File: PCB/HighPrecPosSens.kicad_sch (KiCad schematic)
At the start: 46 parts

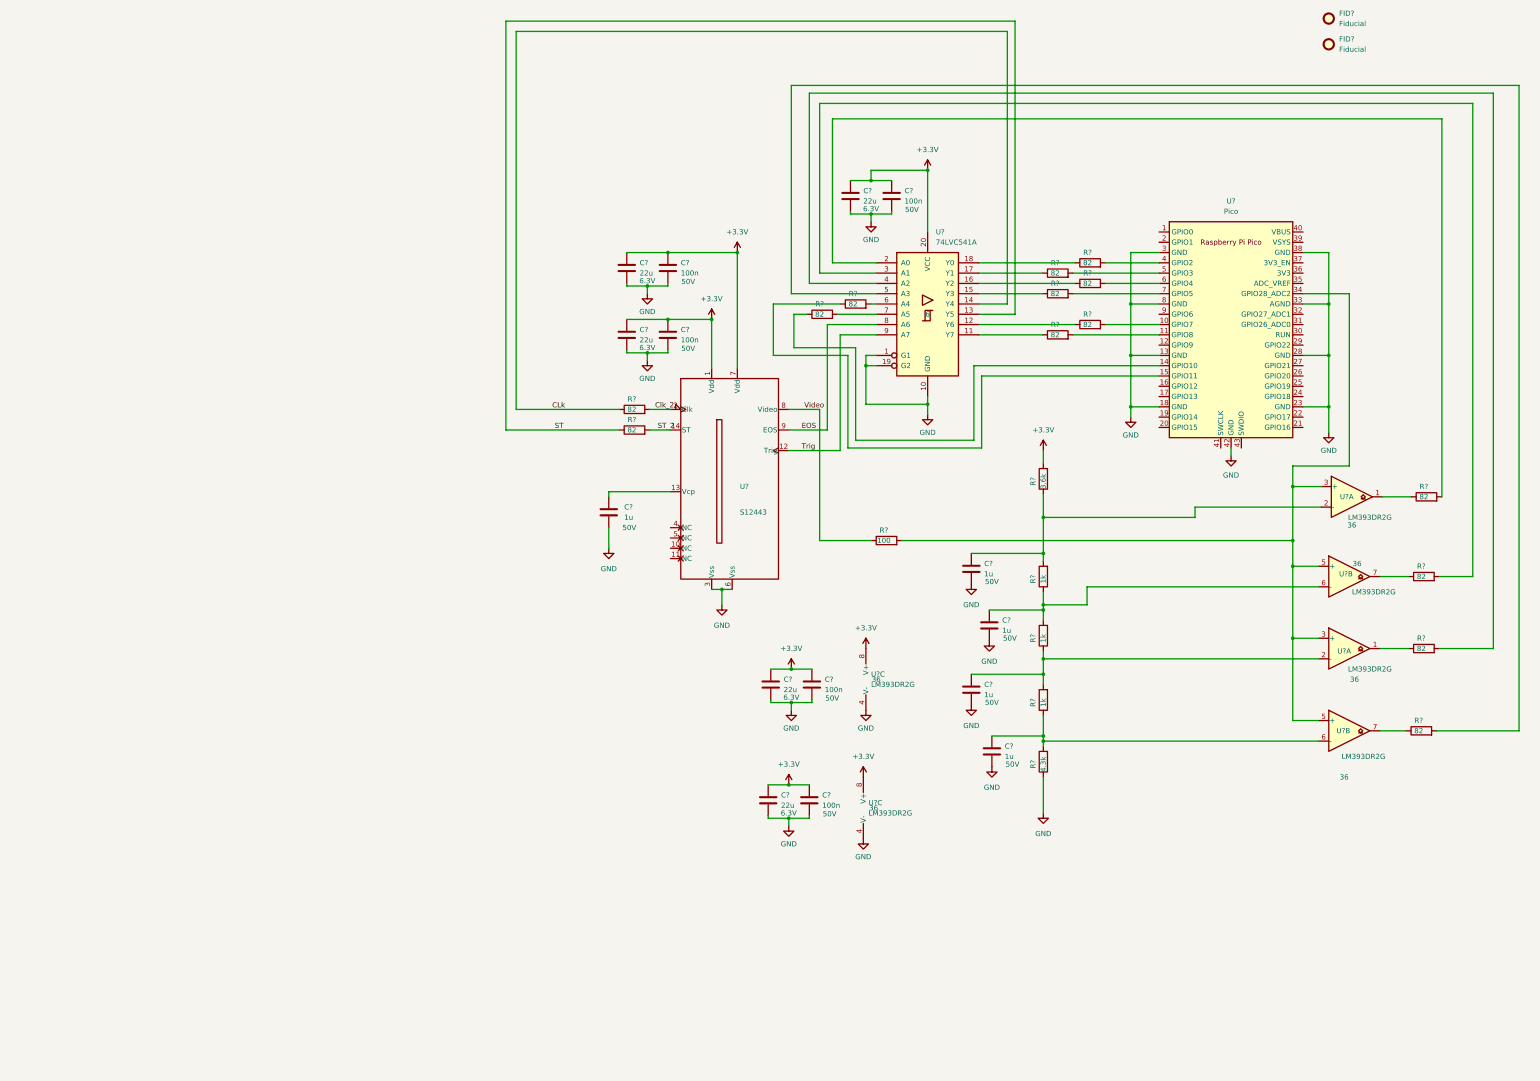
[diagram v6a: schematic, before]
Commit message: added some power supply
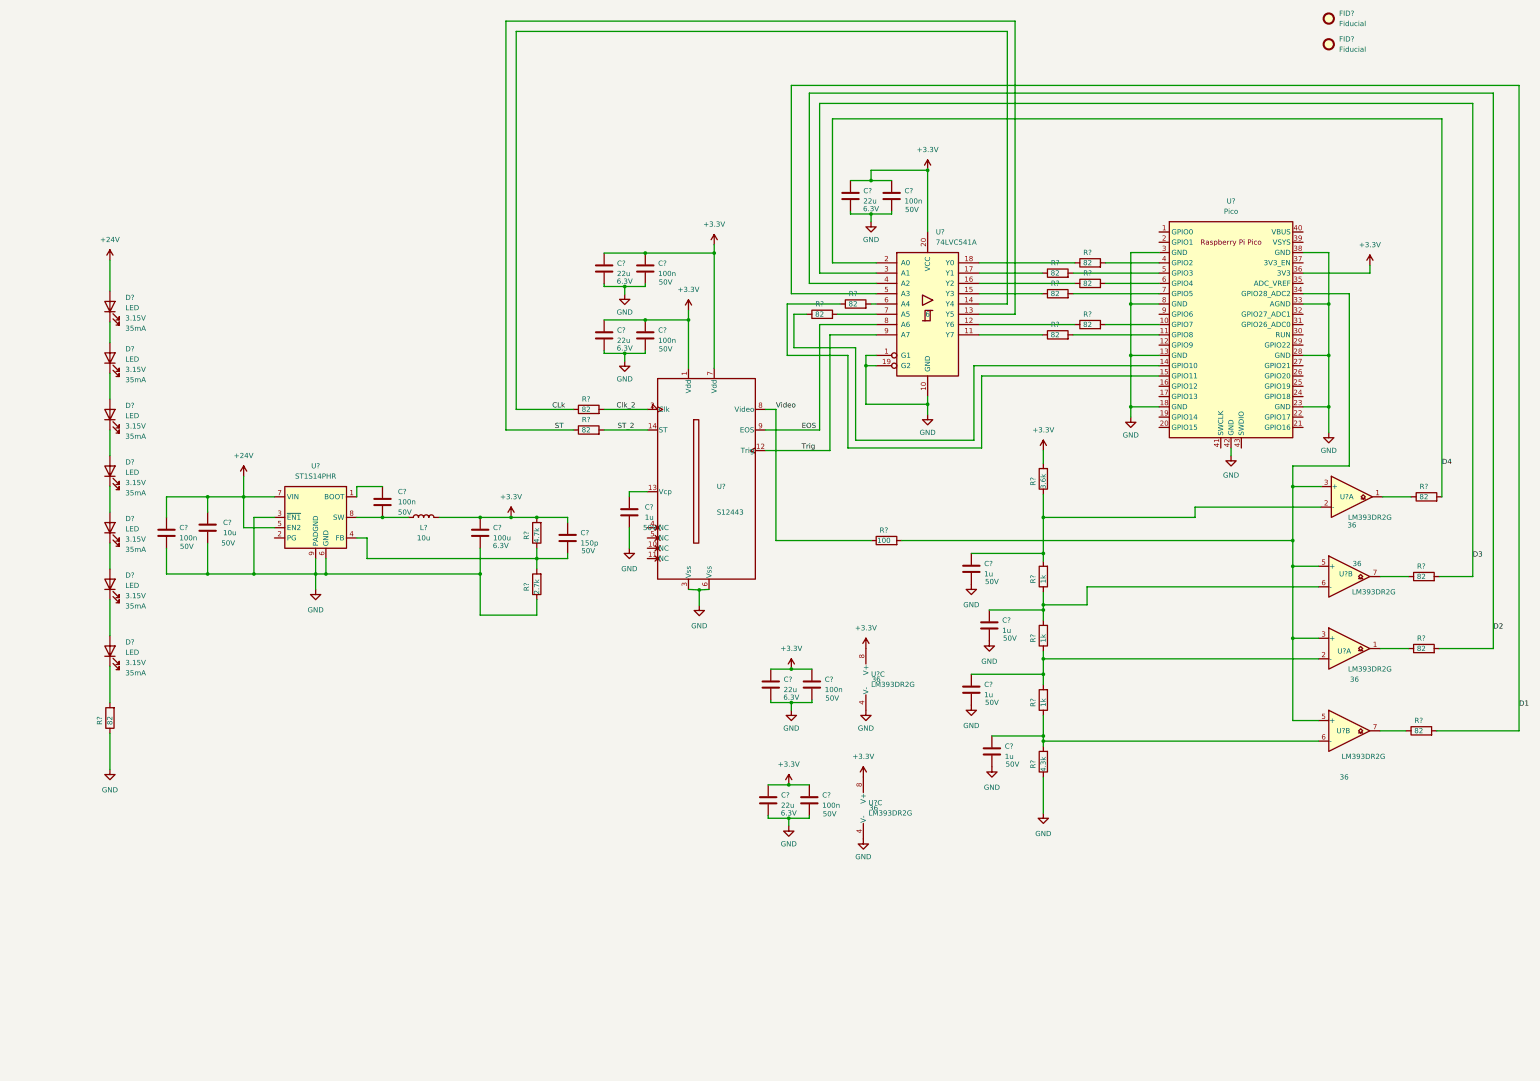
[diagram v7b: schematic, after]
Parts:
- added C?: 150p, Capacitor_SMD:C_0603_1608Metric, symbol Device:C
- added C?: 100u, Capacitor_SMD:C_1206_3216Metric_Pad1.33x1.80mm_HandSolder, symbol Device:C
- added C? (x2): 100n, Capacitor_SMD:C_0603_1608Metric, symbol Device:C
- added C?: 10u, Capacitor_SMD:C_0805_2012Metric_Pad1.18x1.45mm_HandSolder, symbol Device:C
- added D? (x7): LED, symbol Device:LED
- added L?: 10u, Inductor_SMD:L_Taiyo-Yuden_NR-50xx_HandSoldering, symbol Device:L
- added R?: 82, Resistor_SMD:R_0603_1608Metric, symbol Device:R
- added R?: 4.7k, Resistor_SMD:R_0603_1608Metric, symbol Device:R
- added R?: 2.7k, Resistor_SMD:R_0603_1608Metric, symbol Device:R
- added U?: ST1S14PHR, Package_SO:TI_SO-PowerPAD-8, symbol Regulator_Switching:ST1S14PHR
- U?: Manufacturer (none) -> rpi
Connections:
- net +3.3V: now also U?.36 (3V3), C?.1, C?.1, L?.2, R?.2
- net GND: now also C?.2, C?.2, C?.2, R?.1, R?.1, U?.3 (~{EN1}), U?.6 (GND), U?.9 (PADGND)
- net D1: now reaches R?.2, U?.5 (A3)
- net D4: now reaches R?.2, U?.2 (A0)
- net D2: now reaches R?.2, U?.4 (A2)
- net D3: now reaches R?.2, U?.3 (A1)
- new net: D?.1 (K), D?.2 (A) (x6)
- new net: C?.1, U?.1 (BOOT)
- new net: C?.2, R?.1, R?.2, U?.4 (FB)
- new net: C?.2, L?.1, U?.8 (SW)
- new net: D?.1 (K), R?.2
- new net +24V: C?.1, C?.1, D?.2 (A), U?.5 (EN2), U?.7 (VIN)
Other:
- moved on the sheet: C?, R?, U?

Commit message: added some pullups and positioned power supply better
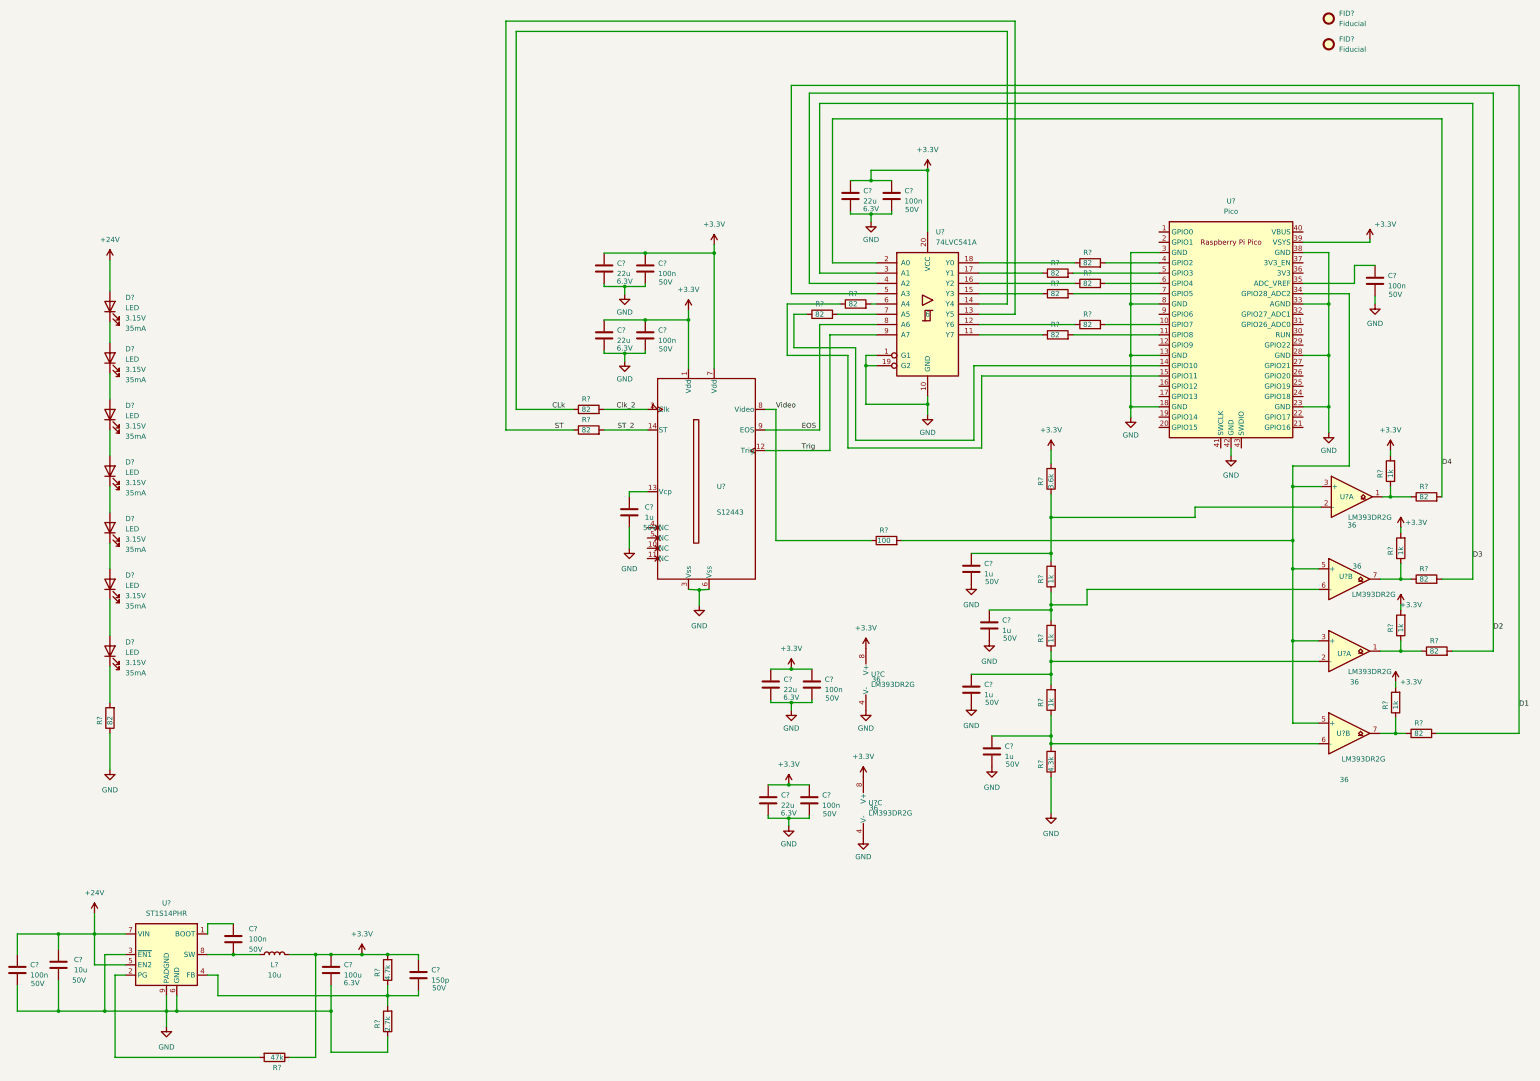
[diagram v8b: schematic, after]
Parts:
- added C?: 100n, Capacitor_SMD:C_0603_1608Metric, symbol Device:C
- added R? (x4): 1k, Resistor_SMD:R_0603_1608Metric, symbol Device:R
- added R?: 47k, Resistor_SMD:R_0603_1608Metric, symbol Device:R
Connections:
- net +3.3V: now also U?.39 (VSYS), R?.1, R?.2, R?.2, R?.2, R?.2; no longer U?.36 (3V3)
- net GND: now also C?.2
- net at U?.2 (PG): now also R?.2
- net at R?.1, U?.7: now also R?.1 (x2)
- net at U?.35 (ADC_VREF): now also C?.1
- net at R?.1, U?.1: now also R?.1 (x2)
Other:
- moved on the sheet: C?, L?, R?, U?, U?A, U?B
